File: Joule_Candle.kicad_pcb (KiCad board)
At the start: 2 copper layers, 14 x 80 mm, 7 parts, among them Q1 BC817-40

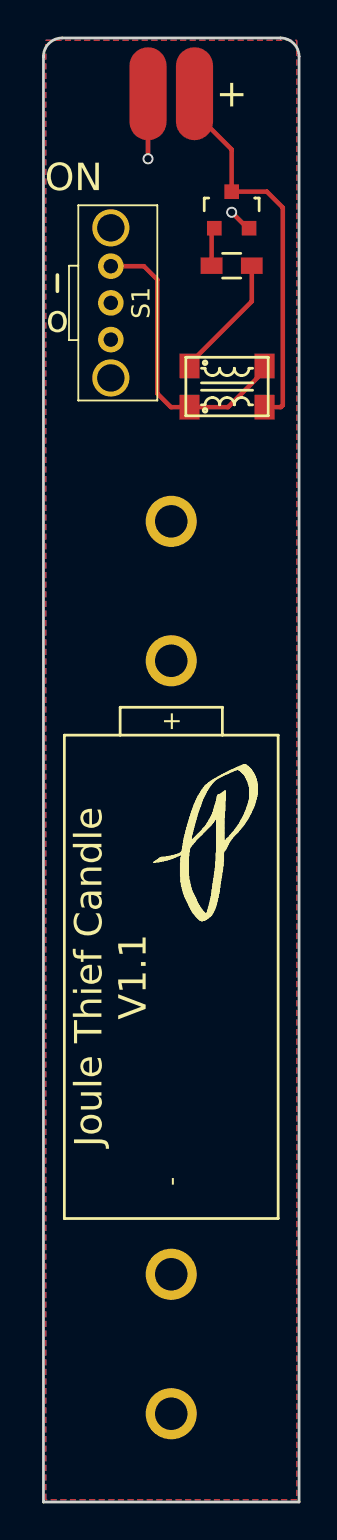
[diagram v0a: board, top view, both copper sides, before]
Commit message: update silkscreen version
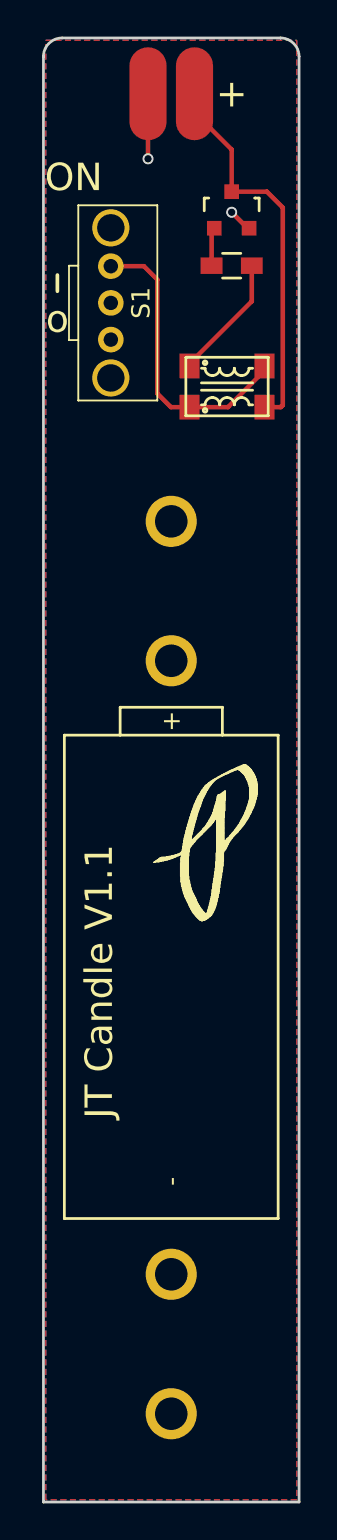
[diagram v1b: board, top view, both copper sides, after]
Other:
- board text added: "JT Candle V1.1"
- board text removed: "Joule Thief Candle V1.1"
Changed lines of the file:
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@@
     (links 11)
     (no_connects 0)
-    (area 152.949 51.740999 170.069715 131.901001)
+    (area 153.975999 51.740999 168.096001 131.901001)
     (thickness 1.6)
     (drawings 38)
@@
     (nets 8)
   )
-  (page A4)
+  (page A)
   (layers
     (0 F.Cu signal)
     (31 B.Cu signal)
-    (32 B.Adhes user hide)
-    (33 F.Adhes user hide)
-    (34 B.Paste user hide)
-    (35 F.Paste user hide)
+    (32 B.Adhes user)
+    (33 F.Adhes user)
+    (34 B.Paste user)
+    (35 F.Paste user)
     (36 B.SilkS user)
     (37 F.SilkS user)
     (38 B.Mask user)
     (39 F.Mask user)
-    (40 Dwgs.User user hide)
-    (41 Cmts.User user hide)
-    (42 Eco1.User user hide)
-    (43 Eco2.User user hide)
+    (40 Dwgs.User user)
+    (41 Cmts.User user)
+    (42 Eco1.User user)
+    (43 Eco2.User user)
     (44 Edge.Cuts user)
     (45 Margin user)
-    (46 B.CrtYd user hide)
-    (47 F.CrtYd user hide)
-    (48 B.Fab user hide)
-    (49 F.Fab user hide)
+    (46 B.CrtYd user)
+    (47 F.CrtYd user)
+    (48 B.Fab user)
+    (49 F.Fab user)
   )
   (setup
@@
     (pad_to_mask_clearance 0.2)
     (aux_axis_origin 0 0)
-    (visible_elements 7FFCFFFF)
+    (visible_elements 7FFFFFFF)
     (pcbplotparams
       (layerselection 0x010f0_80000001)
@@
       (net 3 "Net-(D1-Pad2)"))
   )
+  (gr_text "JT Candle V1.1" (at 157.099 103.378 90) (layer F.SilkS)
+    (effects (font (size 1.5 1.5) (thickness 0.3)))
+  )
   (gr_text + (at 164.338 54.864) (layer F.SilkS)
     (effects (font (size 1.5 1.5) (thickness 0.3)))
@@
   (gr_arc (start 161.798 60.325) (end 162.306 60.325) (angle 90) (layer B.SilkS) (width 0.2))
   (gr_arc (start 161.798 60.325) (end 161.798 60.833) (angle 90) (layer B.SilkS) (width 0.2))
-  (gr_text "Joule Thief Candle\nV1.1" (at 157.734 103.124 90) (layer F.SilkS)
-    (effects (font (size 1.5 1.5) (thickness 0.3)))
-  )
   (gr_line (start 154.813 65.659) (end 154.813 64.77) (angle 90) (layer F.SilkS) (width 0.2))
   (gr_text o (at 154.813 67.183) (layer F.SilkS)
